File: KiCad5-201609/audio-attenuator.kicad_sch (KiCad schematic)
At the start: 44 parts, among them K201 CINCH-DUAL, K202 CINCH-DUAL, K203 CINCH-DUAL, K204 CINCH-DUAL, K207 RELAY_G6K, K208 RELAY_G6K, K209 RELAY_G6K, K210 RELAY_G6K, K211 RELAY_G6K, K212 RELAY_G6K, K213 RELAY_G6K_AB, K214 RELAY_G6K_AB, K215 RELAY_G6K_AB, K216 RELAY_G6K_AB, P1 audioIn, P2 audioOut

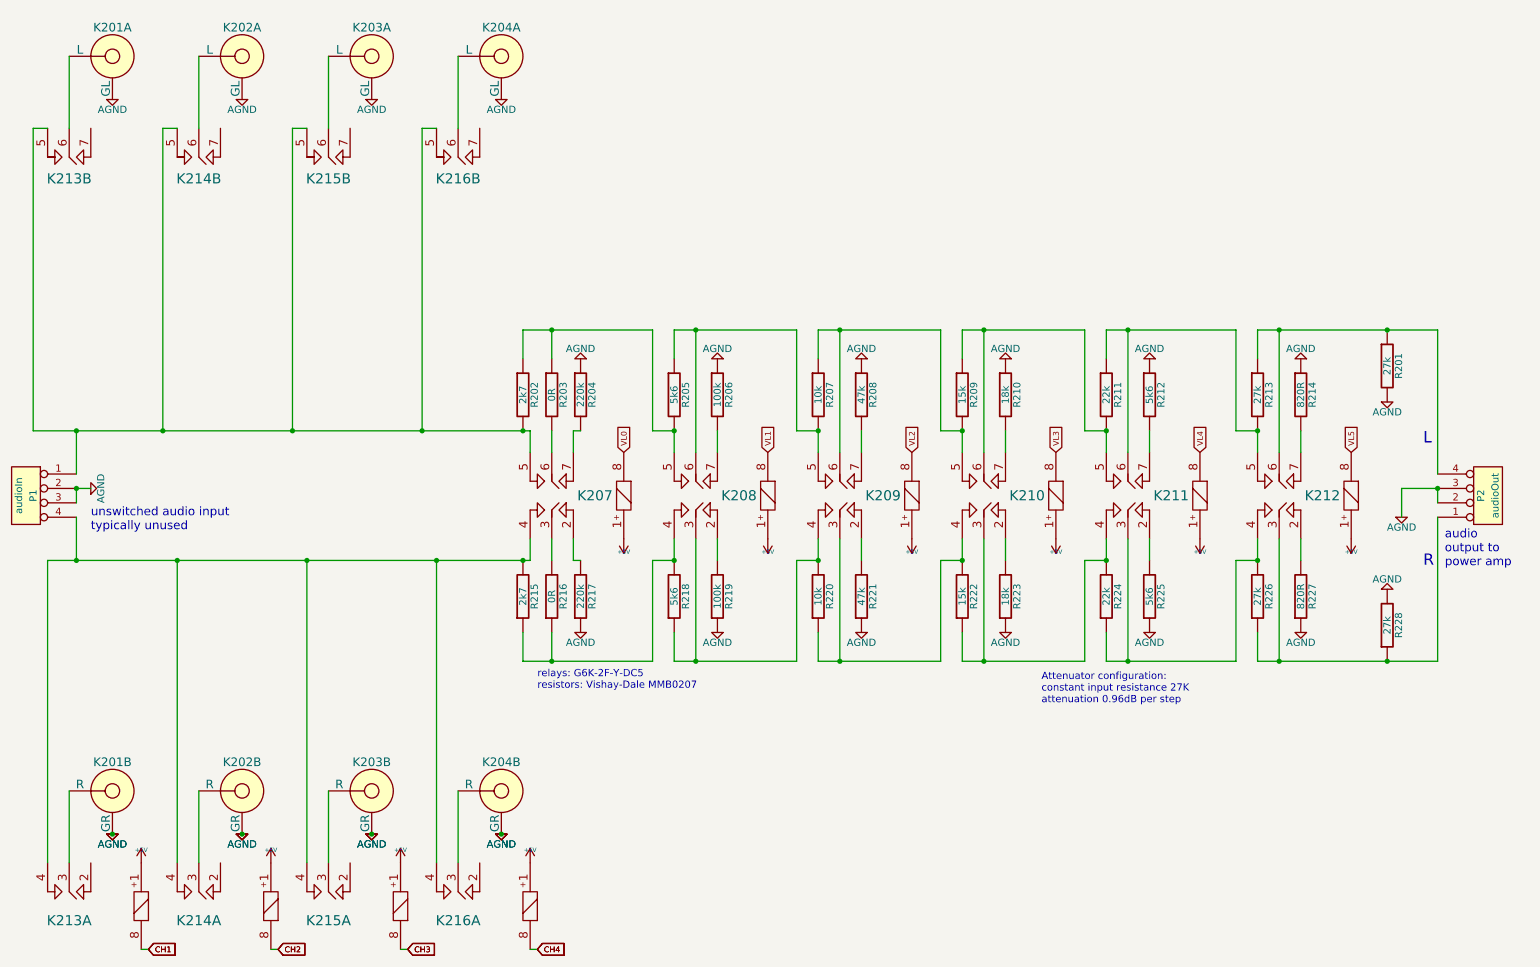
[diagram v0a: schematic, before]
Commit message: moved control to side, added electrolytic caps
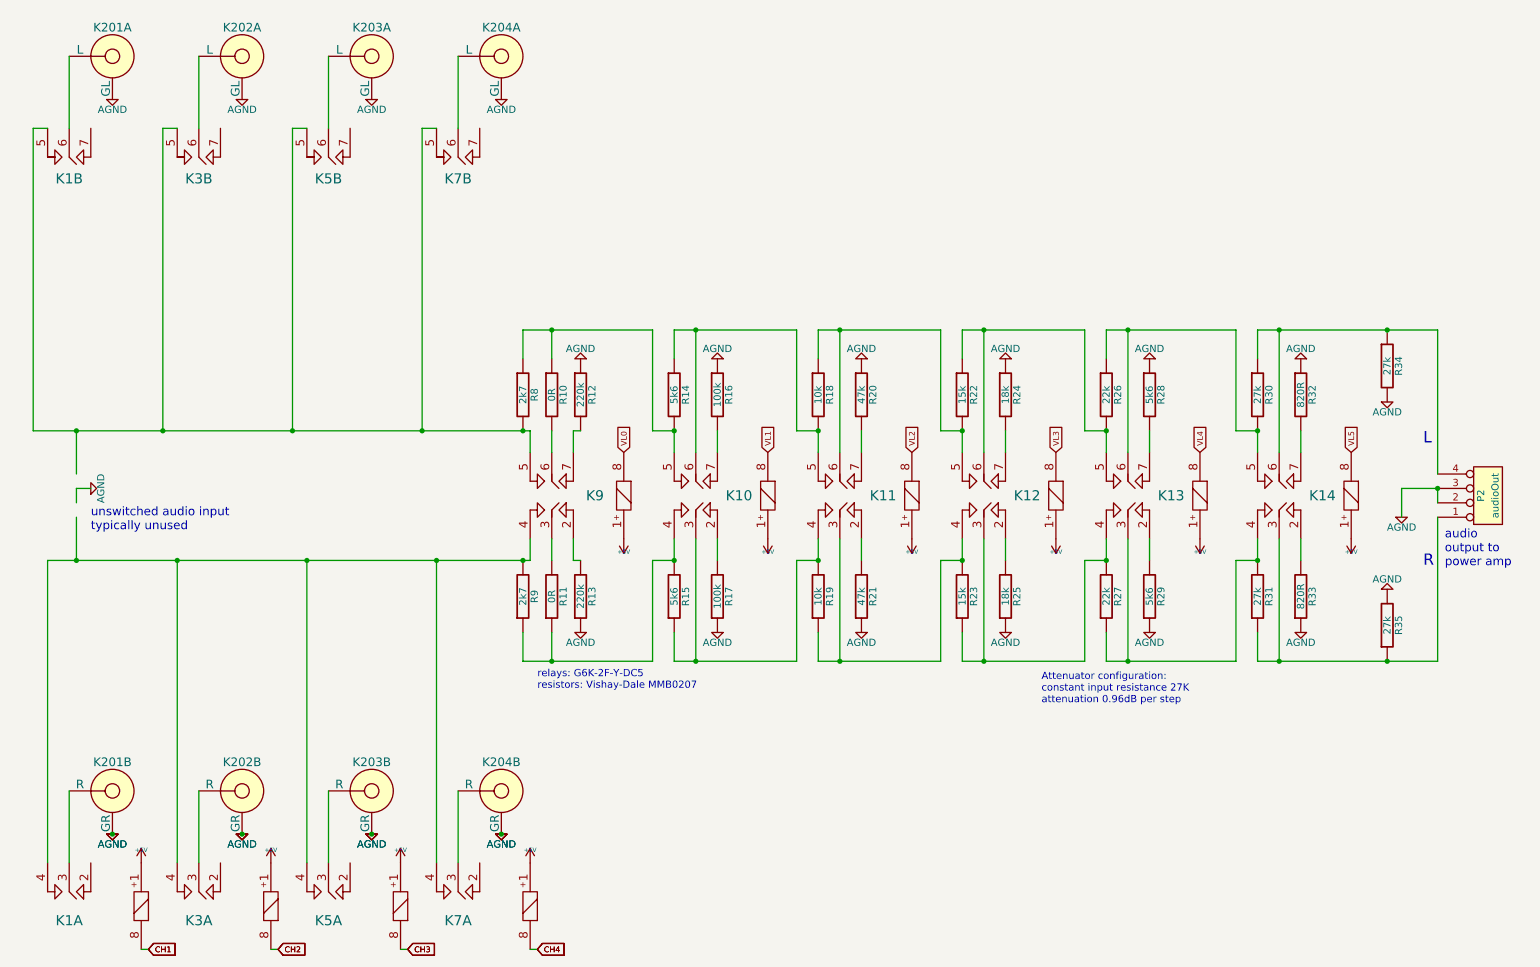
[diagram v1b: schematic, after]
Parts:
- removed P1: audioIn, RlxPassiveFootprints:PIN_ARRAY_4x1, symbol relaixedPassive-rescue:CONN_4
- renumbered K213 to K1, K208 to K10, K209 to K11, K210 to K12, K211 to K13, K212 to K14, K214 to K3, K215 to K5, K216 to K7, K207 to K9, R203 to R10, R216 to R11, R204 to R12, R217 to R13, R205 to R14, R218 to R15, R206 to R16, R219 to R17, R207 to R18, R220 to R19, R208 to R20, R221 to R21, R209 to R22, R222 to R23, R210 to R24, R223 to R25, R211 to R26, R224 to R27, R212 to R28, R225 to R29, R213 to R30, R226 to R31, R214 to R32, R227 to R33, R201 to R34, R228 to R35, R202 to R8, R215 to R9

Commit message: added output rca option
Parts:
- added K? (x2): CINCH-DUAL, RlxPassiveFootprints:switchcraft-dualcinch, symbol relaixedPassive-rescue:cinch-dual
- added P1, P?: audioIn, RlxPassiveFootprints:PIN_ARRAY_4x1, symbol relaixedPassive-rescue:CONN_4
- renumbered R16 to R10, R17 to R11, R18 to R12, R19 to R13, R20 to R14, R21 to R15, R22 to R16, R23 to R17, R24 to R18, R25 to R19, R8 to R2, R26 to R20, R27 to R21, R28 to R22, R29 to R23, R30 to R24, R31 to R25, R32 to R26, R33 to R27, R34 to R28, R35 to R29, R9 to R3, R10 to R4, R11 to R5, R12 to R6, R13 to R7, R14 to R8, R15 to R9
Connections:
- net AGND: now also K?.3 (GL), K?.4 (GR), P1.2 (P2), P1.3 (P3), P?.2 (P2), P?.3 (P3)
- net at K1.5, K3.5, K5.5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: now also P1.1 (P1)
- net at K1.4, K3.4, K5.4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: now also P1.4 (P4)
- new net: K?.2 (L), P?.1 (P1)
- new net: K?.1 (R), P?.4 (P4)
